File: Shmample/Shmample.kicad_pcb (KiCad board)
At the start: 2 copper layers, 127 x 127 mm, 149 parts, among them J1 Conn_01x04_Socket, J2 PowerOut, Q1 BC547, Q10 BC547, Q2 BC557, Q3 BC547, Q4 BC547, Q5 BC557, Q6 BC557, Q7 BC547, Q8 BC557, Q9 BC547, U1 358, U2 40106, U3 4015, U4 4066, U5 324, U6 LM7809_TO220, U7 4052, U8 358

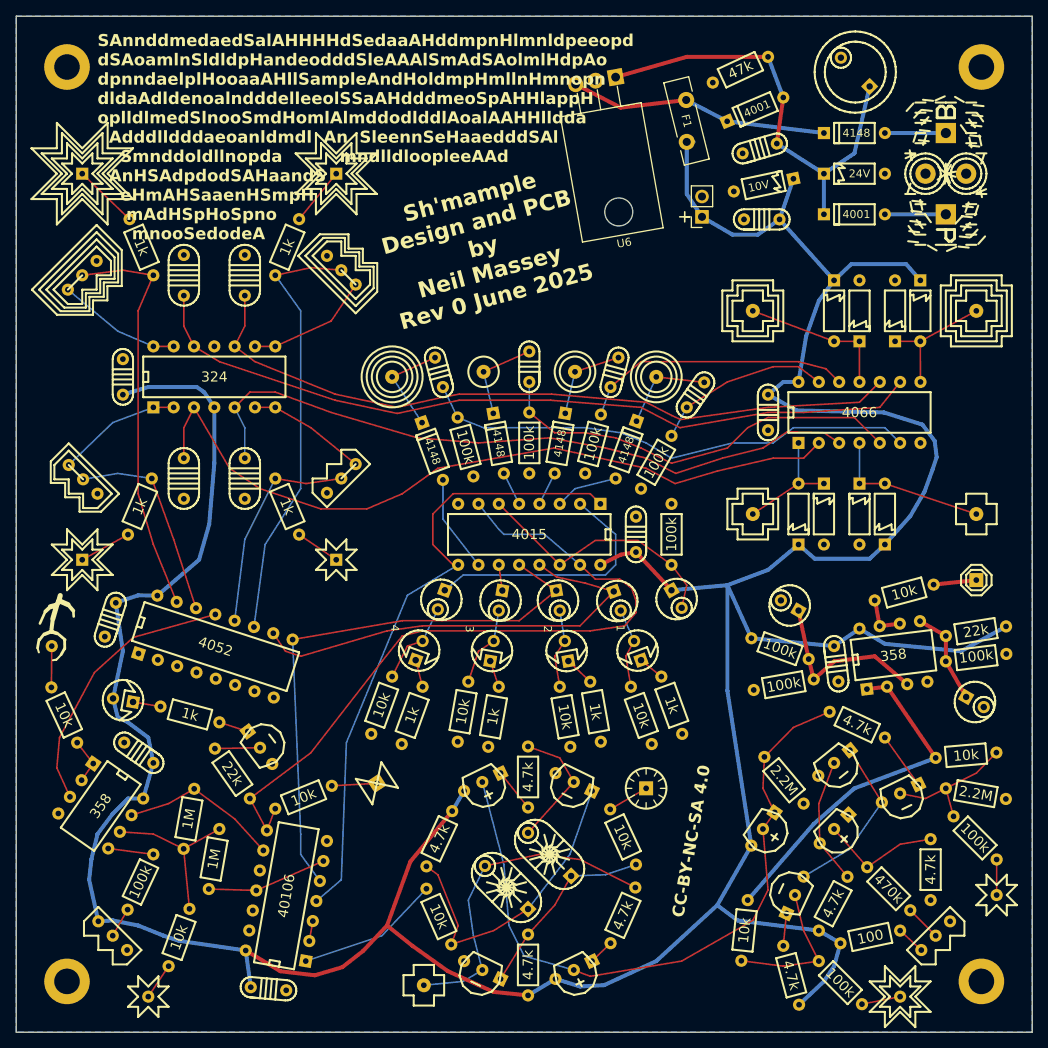
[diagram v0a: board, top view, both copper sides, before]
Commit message: ironed out some kinky tracks
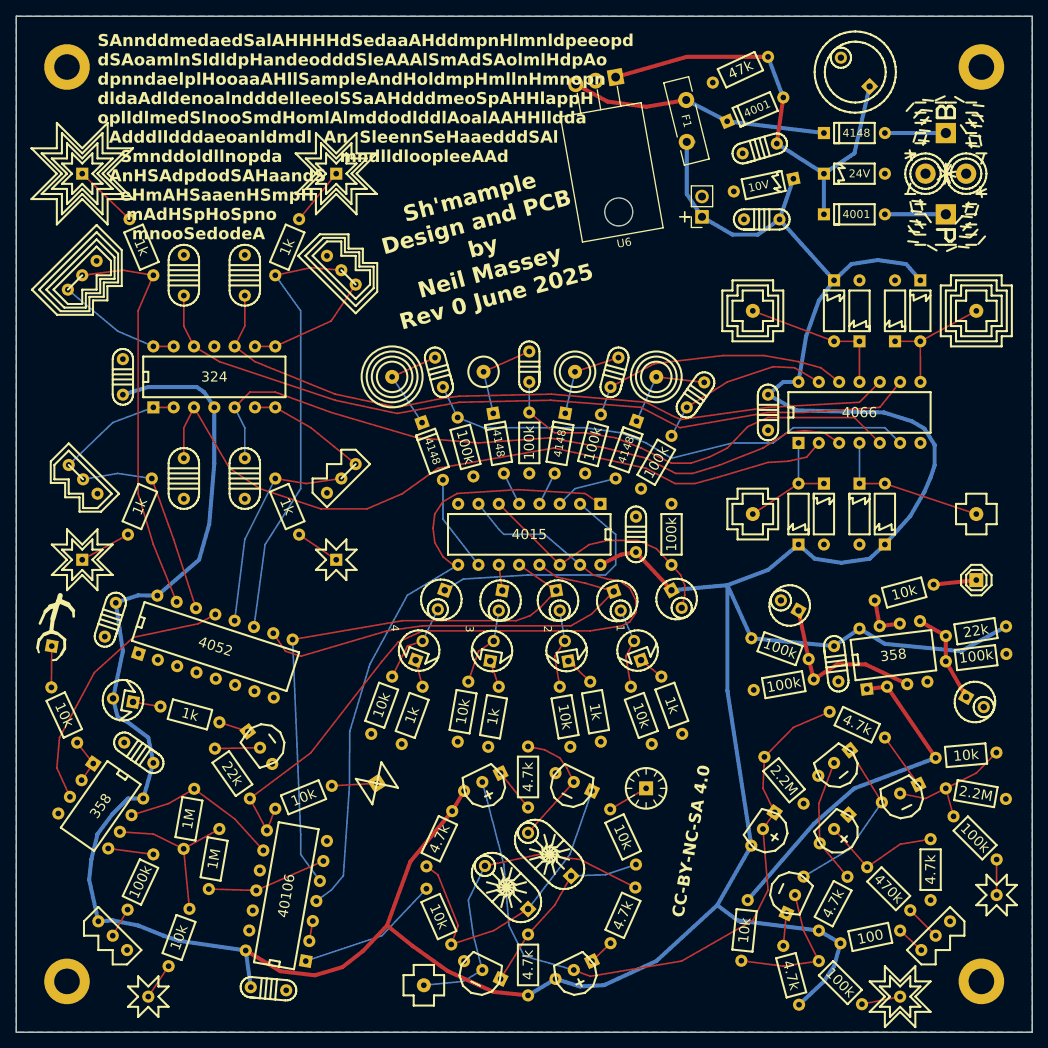
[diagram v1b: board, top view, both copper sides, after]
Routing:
- net Net-(U1A-+): track 22.7 -> 21.6 mm
- net Data: track 92.2 -> 91.6 mm

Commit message: Revision 1
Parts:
- removed C25, C26: 10uF, diy-nabra:cel1
- removed C27, C28: 100nF, diy-nabra:cpoly104_small
- removed J2: PowerOut, Connector_PinSocket_2.54mm:PinSocket_1x02_P2.54mm_Vertical
- removed TP20: Clk-Out, diy-nabra:wclk_out
- added C18: 10nF, diy-nabra:cpoly103, F.Cu at (93.3, 74.3)
- added D23: 9V1, diy-nabra:doz3, F.Cu at (102.9, 52.1)
- added PowerPos1: ThePowerOut, Connector_PinSocket_2.54mm:PinSocket_1x02_P2.54mm_Vertical, F.Cu at (105.4, 27.9)
- added Q11: BC547, diy-nabra:qnpn, F.Cu at (18.4, 87.0)
- added Q12: BC547, diy-nabra:qnpn, F.Cu at (18.4, 116.2)
- added Q13: BC547, diy-nabra:qnpn, F.Cu at (45.7, 117.5)
- added Q14: BC547, diy-nabra:qnpn, F.Cu at (18.4, 124.5)
- added R40: 100k, diy-nabra:r3, F.Cu at (43.2, 104.1)
- added R51: 100k, diy-nabra:r3, F.Cu at (73.0, 118.1)
- added R52: 47k, diy-nabra:r3, F.Cu at (82.5, 118.7)
- added R53: 22k, diy-nabra:r3, F.Cu at (79.4, 118.1)
- added R54: 10k, diy-nabra:r3, F.Cu at (76.2, 117.5)
- added R55: 1M, diy-nabra:r3, F.Cu at (63.8, 112.9)
- added R56: 22k, diy-nabra:r3, F.Cu at (23.5, 121.3)
- added R57: 1M, diy-nabra:r3, F.Cu at (67.7, 111.4)
- added R58: 1k, diy-nabra:r3, F.Cu at (31.1, 124.5)
- added R59: 22k, diy-nabra:r3, F.Cu at (88.6, 112.9)
- added R60: 10k, diy-nabra:r3, F.Cu at (88.9, 121.3)
- added R61: 1k, diy-nabra:r3, F.Cu at (61.0, 36.8)
- added R62: 1k, diy-nabra:r3, F.Cu at (73.7, 36.8)
- added R63: 1k, diy-nabra:r3, F.Cu at (86.4, 36.8)
- added R64: 1k, diy-nabra:r3, F.Cu at (99.1, 36.8)
- added R65: 10k, diy-nabra:r3, F.Cu at (57.7, 129.1)
- added R66: 100k, diy-nabra:r3, F.Cu at (96.4, 131.4)
- added R67: 100k, diy-nabra:r3, F.Cu at (87.6, 129.5)
- added R68: 100, diy-nabra:r3, F.Cu at (59.7, 50.2)
- added R69: 100, diy-nabra:r3, F.Cu at (73.0, 50.2)
- added R70: 100, diy-nabra:r3, F.Cu at (86.4, 50.2)
- added R71: 100, diy-nabra:r3, F.Cu at (100.3, 50.2)
- C1: value 10uF -> 2200uF; footprint diy-nabra:cel1 -> diy-nabra:cel2
- C10, C12: value 1uF -> *; footprint diy-nabra:cpoly105 -> diy-nabra:chairy
- C11, C9: value 1uF -> 10uF; footprint diy-nabra:cpoly105 -> diy-nabra:cel1
- C13: value 100nF -> 10uF; footprint diy-nabra:cpoly104_small -> diy-nabra:cel1
- C15, C16: value 100nF -> 10nF; footprint diy-nabra:cpoly104_small -> diy-nabra:cpoly103
- C17: value 10uF -> 10nF; footprint diy-nabra:cel1 -> diy-nabra:cpoly103
- C19: value 2200uF -> 1uF; footprint diy-nabra:cel2 -> diy-nabra:cpoly105
- C20, C21: value 100nF -> 1uF; footprint diy-nabra:cpoly104_small -> diy-nabra:cpoly105
- C22: value 10uF -> 1uF; footprint diy-nabra:cel1 -> diy-nabra:cpoly105
- C23: value 10uF -> 100nF; footprint diy-nabra:cel1 -> diy-nabra:cpoly104_small
- C3, C8: value * -> 100nF; footprint diy-nabra:chairy -> diy-nabra:cpoly104_small
- C4, C5, C6, C7: value 10nF -> 100nF; footprint diy-nabra:cpoly103 -> diy-nabra:cpoly104_small
- D1, D3: value LED -> 4001; footprint diy-nabra:led -> diy-nabra:do3
- D10, D12, D13: value 4148 -> LED; footprint diy-nabra:do3 -> diy-nabra:led
- D11: value 10V -> LED; footprint diy-nabra:doz3 -> diy-nabra:led
- D15: value 9V1 -> LED; footprint diy-nabra:doz3 -> diy-nabra:led
- D2: value LED -> 24V; footprint diy-nabra:led -> diy-nabra:doz3
- D4: value LED -> 4148; footprint diy-nabra:led -> diy-nabra:do3
- D5: value LED -> 10V; footprint diy-nabra:led -> diy-nabra:doz3
- D6, D7: value 4001 -> 4148
- D8: value 24V -> 4148; footprint diy-nabra:doz3 -> diy-nabra:do3
- R1: value 100k -> 47k
- R10, R29: value 4.7k -> 10k
- R11: value 1M -> 2.2M
- R12: value 4.7k -> 100k
- R13: value 10k -> 2.2M
- R14: value 2.2M -> 4.7k
- R16: value 2.2M -> 100k
- R19, R8: value 10k -> 4.7k
- R2: value 470k -> 100
- R20: value 4.7k -> 22k
- R22, R23: value 100k -> 10k
- R25, R26, R27, R28: value 1k -> 100k
- R30: value 22k -> 10k
- R31: value 47k -> 10k
- R32, R33, R34, R35, R36: value 1k -> 10k
- R37: value 22k -> 100k
- R39, R49, R50: value 10k -> 100k
- R4: value 100k -> 470k
- R41: value 100 -> 10k
- R45, R48: value 10k -> 1k
- R46: value 1M -> 1k
- R47: value 100k -> 1k
- R7: value 100k -> 4.7k
- RV3: value 4_W -> 1_W; footprint diy-nabra:wnob4 -> diy-nabra:wnob1
- RV4: value 3_W -> 2_W; footprint diy-nabra:wnob3 -> diy-nabra:wnob2
- RV5: value 2_W -> 3_W; footprint diy-nabra:wnob2 -> diy-nabra:wnob3
- RV6: value 1_W -> 4_W; footprint diy-nabra:wnob1 -> diy-nabra:wnob4
- TP10: value In-4 -> Rung; footprint diy-nabra:wsqu4in -> diy-nabra:wsqout
- TP11: value Out-4 -> In-1; footprint diy-nabra:wtrin4 -> diy-nabra:wsquin
- TP12: value Cmp-Out -> In-2; footprint diy-nabra:wcmp_out -> diy-nabra:wsqu2in
- TP13: value Hi -> In-3; footprint diy-nabra:wvout -> diy-nabra:wsqu3in
- TP14: value Pls-1 -> In-4; footprint diy-nabra:wcircin -> diy-nabra:wsqu4in
- TP15: value Pls-2 -> Out-1; footprint diy-nabra:wcirc2in -> diy-nabra:wtrin
- TP16: value Pls-3 -> Out-2; footprint diy-nabra:wcirc3in -> diy-nabra:wtrin2
- TP17: value Pls-4 -> Out-3; footprint diy-nabra:wcirc4in -> diy-nabra:wtrin3
- TP18: value Brown -> Out-4; footprint diy-nabra:wsquin -> diy-nabra:wtrin4
- TP19: footprint diy-nabra:wpod -> diy-nabra:wsqout
- TP2: value Data -> Ver
- TP3: value Ver -> Brown; footprint diy-nabra:wtrin -> diy-nabra:wsquin
- TP4: value In-1 -> Hi; footprint diy-nabra:wsquin -> diy-nabra:wvout
- TP5: value Out-1 -> Pls-1; footprint diy-nabra:wtrin -> diy-nabra:wcircin
- TP6: value In-3 -> Pls-2; footprint diy-nabra:wsqu2in -> diy-nabra:wcirc2in
- TP7: value Out-2 -> Pls-3; footprint diy-nabra:wtrin2 -> diy-nabra:wcirc3in
- TP8: value In-2 -> Pls-4; footprint diy-nabra:wsqu3in -> diy-nabra:wcirc4in
- TP9: value Out-3 -> Data; footprint diy-nabra:wtrin3 -> diy-nabra:wtrin
- U1: value 358 -> LM7809_TO220; footprint diy-nabra:dip8 -> Package_TO_SOT_THT:TO-220F-3_Horizontal_TabDown
- U2: value 40106 -> 358; footprint diy-nabra:dip14 -> diy-nabra:dip8
- U3: value 4015 -> 4066; footprint diy-nabra:dip16 -> diy-nabra:dip14
- U4: value 4066 -> LM324
- U5: value 324 -> 40106
- U6: value LM7809_TO220 -> LM324; footprint Package_TO_SOT_THT:TO-220-3_Horizontal_TabDown -> diy-nabra:dip14
- U7: value 4052 -> 4015
- U8: value 358 -> 4052; footprint diy-nabra:dip8 -> diy-nabra:dip16
- moved H1 161.6 mm to (133.3, 133.3)
- moved H2 161.6 mm to (19.1, 133.3)
- moved H3 114.3 mm to (133.3, 19.1)
- moved H4 114.3 mm to (19.1, 19.1)
- moved TP18 109.3 mm to (95.2, 29.2), turned to 0 degrees
- moved R38 108.8 mm to (20.3, 100.3), turned to 105 degrees
- moved C11 107.7 mm to (133.6, 97.9), turned to 115 degrees
- moved TP9 105.5 mm to (26.7, 134.6), turned to 90 degrees
- moved R1 103.7 mm to (109.3, 27.1), turned to -6 degrees
- moved D5 99.9 mm to (109.7, 42.0), turned to 20 degrees
- moved D15 97.8 mm to (36.1, 124.3), turned to 115 degrees
- moved TP2 96.5 mm to (125.7, 134.6)
- moved R37 93.9 mm to (43.2, 100.3), turned to 75 degrees
- moved R18 93.4 mm to (121.9, 53.3)
- moved R11 92.8 mm to (129.5, 120.7), turned to -65 degrees
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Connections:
- C1 pad 1: Net-(U1A-+) -> Net-(D1-K)
- C10 pad 1: Net-(U5A-+) -> Net-(Q7-C)
- C10 pad 2: GND -> Net-(Q9-B)
- C11 pad 1: Net-(U5C-+) -> Net-(U2B-+)
- C12 pad 1: Net-(U5D-+) -> Net-(Q9-C)
- C12 pad 2: GND -> Net-(Q7-B)
- C13 pad 1: GND -> +9V
- C13 pad 2: +9V -> RST
- C15 pad 1: GND -> Net-(C15-Pad1)
- C15 pad 2: +9V -> Net-(Q10-B)
- C16 pad 1: GND -> Net-(C16-Pad1)
- C16 pad 2: +9V -> Net-(Q11-B)
- C17 pad 1: Net-(U1B-+) -> Net-(C17-Pad1)
- C17 pad 2: GND -> Net-(Q12-B)
- C19 pad 1: Net-(D6-K) -> Net-(U6C-+)
- C2 pad 1: GND -> Net-(D1-K)
- C2 pad 2: +9V -> GND
- C20 pad 1: Net-(D6-K) -> Net-(U6D-+)
- C21 pad 1: +9V -> Net-(U6A-+)
- C22 pad 1: Q1 -> Net-(U6B-+)
- C22 pad 2: Net-(D1-A) -> GND
- C23 pad 1: Q2 -> +9V
- C23 pad 2: Net-(D2-A) -> GND
- C24 pad 1: Net-(U3B-Q3) -> Net-(U4B-+)
- C24 pad 2: Net-(D3-A) -> GND
- C3 pad 1: Net-(Q7-C) -> +9V
- C3 pad 2: Net-(Q9-B) -> GND
- C4 pad 1: Net-(D10-K) -> GND
- C4 pad 2: SW1 -> +9V
- C5 pad 1: Net-(D12-K) -> GND
- C5 pad 2: SW2 -> +9V
- C6 pad 1: Net-(D13-K) -> GND
- C6 pad 2: SW3 -> +9V
- C7 pad 1: Net-(D14-K) -> GND
- C7 pad 2: SW4 -> +9V
- C8 pad 1: Net-(Q9-C) -> GND
- C8 pad 2: Net-(Q7-B) -> +9V
- C9 pad 1: Net-(U5B-+) -> Net-(U2A-+)
- D10 pad 1: Net-(D10-K) -> GND
- D11 pad 1: +9V -> GND
- D11 pad 2: GND -> Net-(D11-A)
- D12 pad 1: Net-(D12-K) -> GND
- D13 pad 1: Net-(D13-K) -> GND
- D15 pad 2: GND -> +9V
- D16 pad 2: Net-(D15-K) -> Net-(D16-A)
- D17 pad 1: +9V -> Net-(D16-A)
- D17 pad 2: Net-(D17-A) -> GND
- D18 pad 1: Net-(D17-A) -> +9V
- D18 pad 2: GND -> Net-(D18-A)
- D19 pad 1: +9V -> Net-(D18-A)
- D19 pad 2: Net-(D19-A) -> GND
- D2 pad 1: Net-(D2-K) -> Net-(D1-K)
- D2 pad 2: Net-(D2-A) -> GND
- D20 pad 1: Net-(D19-A) -> +9V
- D20 pad 2: GND -> Net-(D20-A)
- D21 pad 1: +9V -> Net-(D20-A)
- D21 pad 2: Net-(D21-A) -> GND
- D22 pad 1: Net-(D21-A) -> +9V
- D22 pad 2: GND -> Net-(D22-A)
- D3 pad 2: Net-(D3-A) -> Net-(D1-K)
- D4 pad 1: Net-(D4-K) -> Net-(D3-K)
- D4 pad 2: Net-(D4-A) -> Batt
- D5 pad 1: Net-(D5-K) -> +9V
- D5 pad 2: +9V -> GND
- D6 pad 2: Net-(D6-A) -> Q1A
- D7 pad 2: Net-(D6-K) -> Q2A
- D8 pad 1: Net-(D6-K) -> Net-(D8-K)
- D8 pad 2: GND -> Q3A
- D9 pad 1: Net-(D7-K) -> Net-(D9-K)
- D9 pad 2: Batt -> Q4B
- F1 pad 1: Net-(D7-K) -> Net-(D3-K)
- J1 pad 1: Net-(D6-A) -> Net-(D1-A)
- R1 pad 1: Net-(R1-Pad1) -> Net-(D1-K)
- R1 pad 2: Net-(Q1-B) -> GND
- R10 pad 1: Net-(Q2-E) -> Net-(Q4-B)
- R10 pad 2: +9V -> MIDO
- R11 pad 1: Net-(U8B--) -> GND
- R11 pad 2: Net-(R11-Pad2) -> Net-(Q4-B)
- R12 pad 1: Net-(Q4-C) -> Net-(Q4-B)
- R12 pad 2: Net-(Q5-B) -> Net-(R12-Pad2)
- R13 pad 1: Net-(Q4-B) -> GND
- R13 pad 2: MIDO -> Net-(Q5-B)
- R14 pad 1: GND -> Net-(Q7-B)
- R14 pad 2: Net-(Q4-B) -> Net-(Q6-C)
- R15 pad 1: Net-(Q4-B) -> Net-(U2A-+)
- R15 pad 2: Net-(R15-Pad2) -> +9V
- R16 pad 2: Net-(Q5-B) -> Net-(U2A-+)
- R17 pad 1: Net-(Q7-B) -> Net-(Q7-C)
- R17 pad 2: Net-(Q6-C) -> +9V
- R18 pad 1: Net-(Q7-C) -> Net-(Q9-B)
- R18 pad 2: +9V -> Net-(Q8-C)
- R19 pad 2: Pulse -> +9V
- R2 pad 2: Net-(Q2-B) -> +9V
- R20 pad 1: Net-(Q9-B) -> Net-(U2B-+)
- R20 pad 2: Net-(Q8-C) -> +9V
- R21 pad 2: SW1 -> Net-(U2B-+)
- R22 pad 1: GND -> Net-(Q9-C)
- R22 pad 2: SW2 -> Pulse
- R23 pad 1: GND -> Net-(R23-Pad1)
- R23 pad 2: SW3 -> Hi
- R24 pad 2: SW4 -> RST
- R25 pad 1: Net-(D1-K) -> GND
- R25 pad 2: GND -> Net-(D6-K)
- R26 pad 1: Net-(D2-K) -> Net-(D7-K)
- R27 pad 1: Net-(D3-K) -> Net-(D8-K)
- R28 pad 1: Net-(D4-K) -> Net-(D9-K)
- R29 pad 1: Net-(Q9-C) -> Net-(D6-K)
- R29 pad 2: +9V -> Net-(C15-Pad1)
- R3 pad 1: Net-(U1A-+) -> Net-(R3-Pad1)
- R3 pad 2: +9V -> Net-(Q1-B)
- R30 pad 1: Net-(Q10-B) -> Net-(D7-K)
- R30 pad 2: Data -> Net-(C16-Pad1)
- R31 pad 1: Net-(D6-K) -> Net-(D8-K)
- R31 pad 2: GND -> Net-(C17-Pad1)
- R32 pad 1: Net-(Q10-C) -> Net-(D9-K)
- R32 pad 2: Net-(D5-K) -> Net-(C18-Pad1)
- R33 pad 1: Net-(U7-X0) -> Net-(C15-Pad1)
- R34 pad 1: Net-(U7-X1) -> Net-(R34-Pad1)
- R34 pad 2: Net-(R34-Pad2) -> Net-(C16-Pad1)
- R35 pad 1: Net-(U7-X3) -> Net-(R35-Pad1)
- R35 pad 2: Net-(R35-Pad2) -> Net-(C17-Pad1)
- R36 pad 1: Net-(U7-X2) -> Net-(R36-Pad1)
- R36 pad 2: Net-(R36-Pad2) -> Net-(C18-Pad1)
- R37 pad 1: Net-(U1B-+) -> Net-(Q10-B)
- R37 pad 2: +9V -> GND
- R38 pad 1: GND -> Net-(Q11-B)
- R38 pad 2: Net-(U1B-+) -> GND
- R39 pad 1: Net-(Q7-C) -> Net-(Q12-B)
- R39 pad 2: Net-(R39-Pad2) -> GND
- R4 pad 1: GND -> Net-(R4-Pad1)
- R4 pad 2: Net-(U1A-+) -> Net-(Q2-B)
- R41 pad 1: Net-(R41-Pad1) -> Net-(Q10-C)
- R42 pad 1: Net-(D1-A) -> Net-(Q11-C)
- R42 pad 2: GND -> +9V
- R43 pad 1: Net-(D2-A) -> Net-(Q12-C)
- R43 pad 2: GND -> +9V
- R44 pad 1: Net-(D3-A) -> Net-(Q13-C)
- R44 pad 2: GND -> +9V
- R45 pad 1: Net-(D4-A) -> Net-(D10-A)
- R45 pad 2: GND -> Q1B
- R46 pad 1: Net-(U8B--) -> Net-(D11-A)
- R46 pad 2: Net-(R46-Pad2) -> Q2B
- R47 pad 1: GND -> Net-(D12-A)
- R47 pad 2: RST -> Q3B
- R48 pad 1: Net-(U8A--) -> Net-(D13-A)
- R48 pad 2: Net-(R48-Pad2) -> Q4A
- R49 pad 2: Data -> Net-(U4D-+)
- R50 pad 2: Hi -> Net-(U4D--)
- R7 pad 1: Net-(R7-Pad1) -> Net-(Q1-C)
- R7 pad 2: Net-(U8B-+) -> +9V
- R8 pad 1: Net-(R8-Pad1) -> Net-(Q2-E)
- R8 pad 2: Net-(U8B--) -> +9V
- R9 pad 1: Net-(Q1-C) -> Net-(Q4-C)
- R9 pad 2: +9V -> Net-(Q5-B)
- RV1 pad 2: Net-(R2-Pad1) -> Net-(R4-Pad1)
- RV1 pad 3: Net-(R41-Pad1) -> Net-(R2-Pad1)
- RV2 pad 2: Net-(R7-Pad1) -> Net-(R49-Pad1)
- RV3 pad 2: Net-(U7-X2) -> Net-(U8-X0)
- RV3 pad 3: Net-(U5D--) -> Net-(U6C--)
- RV4 pad 2: Net-(U7-X3) -> Net-(U8-X1)
- RV4 pad 3: Net-(U5C--) -> Net-(U6D--)
- RV5 pad 2: Net-(U7-X1) -> Net-(U8-X3)
- RV5 pad 3: Net-(U5A--) -> Net-(U6A--)
- RV6 pad 2: Net-(U7-X0) -> Net-(U8-X2)
- RV6 pad 3: Net-(U5B--) -> Net-(U6B--)
- TP1 pad 1: Net-(R1-Pad1) -> Net-(R3-Pad1)
- TP10 pad 1: Net-(D21-A) -> Net-(R60-Pad1)
- TP11 pad 1: Net-(R36-Pad2) -> IN1
- TP12 pad 1: Net-(R49-Pad1) -> IN2
- TP13 pad 1: Net-(R50-Pad1) -> IN3
- TP14 pad 1: Net-(D10-K) -> IN4
- TP15 pad 1: Net-(D12-K) -> Net-(R61-Pad2)
- TP16 pad 1: Net-(D13-K) -> Net-(R62-Pad2)
- TP17 pad 1: Net-(D14-K) -> Net-(R63-Pad2)
- TP18 pad 1: Net-(Q7-B) -> Net-(R64-Pad2)
- TP19 pad 1: Net-(R48-Pad2) -> Net-(R65-Pad2)
- TP2 pad 1: Net-(R8-Pad1) -> Net-(R12-Pad2)
- TP3 pad 1: Net-(R15-Pad2) -> Net-(Q7-B)
- TP4 pad 1: Net-(D15-K) -> Net-(R23-Pad1)
- TP6 pad 1: Net-(D17-A) -> Net-(R34-Pad1)
- TP7 pad 1: Net-(R34-Pad2) -> Net-(R35-Pad1)
- TP8 pad 1: Net-(D19-A) -> Net-(R36-Pad1)
- TP9 pad 1: Net-(R35-Pad2) -> Net-(R50-Pad1)
- U1 pad 1: MIDO -> Net-(D1-K)
- U1 pad 2: MIDO -> GND
- U1 pad 3: Net-(U1A-+) -> Net-(D3-K)
- U2 pad 1: Pulse -> MIDO
- U2 pad 2: Net-(U2-Pad2) -> MIDO
- U2 pad 3: Net-(U2-Pad2) -> Net-(U2A-+)
- U2 pad 4: Net-(U3A-CP) -> GND
- U2 pad 5: Q2 -> Net-(U2B-+)
- U2 pad 6: Net-(R11-Pad2) -> Hi
- U2 pad 7: GND -> Hi
- U2 pad 8: Data -> +9V
- U3 pad 1: Net-(U3A-CP) -> Net-(D22-A)
- U3 pad 10: Net-(D14-A) -> Net-(U6C-+)
- U3 pad 11: Net-(U3B-Q3) -> Net-(D16-A)
- U3 pad 12: Q2 -> SW1
- U3 pad 13: Q1 -> SW4
- U3 pad 14: RST -> +9V
- U3 pad 2: Net-(U3B-Q4) -> Net-(U6B-+)
- U3 pad 3: Net-(D13-A) -> Net-(U6A-+)
- U3 pad 4: Net-(D12-A) -> Net-(D20-A)
- U3 pad 5: Net-(D10-A) -> SW3
- U3 pad 6: RST -> SW2
- U3 pad 7: Data -> GND
- U3 pad 8: GND -> Net-(D18-A)
- U3 pad 9: Net-(U3A-CP) -> Net-(U6D-+)
- U4 pad 1: Net-(D17-A) -> Net-(U4A--)
- U4 pad 10: Net-(U5C-+) -> MIDO2
- U4 pad 11: Net-(D19-A) -> GND
- U4 pad 12: SW2 -> Net-(U4D-+)
- U4 pad 13: SW3 -> Net-(U4D--)
- U4 pad 14: +9V -> Net-(R57-Pad2)
- U4 pad 2: Net-(U5A-+) -> Net-(U4A--)
- U4 pad 3: Net-(U5B-+) -> Net-(U4A-+)
- U4 pad 4: Net-(D15-K) -> +9V
- U4 pad 5: SW1 -> Net-(U4B-+)
- U4 pad 6: SW4 -> MIDO2
- U4 pad 7: GND -> MIDO2
- U4 pad 8: Net-(D21-A) -> Net-(R59-Pad2)
- U4 pad 9: Net-(U5D-+) -> Net-(U4C--)
- U5 pad 1: Net-(U5A--) -> Net-(Q11-C)
- U5 pad 10: Net-(U5C-+) -> SW4
- U5 pad 11: GND -> Net-(Q13-C)
- U5 pad 12: Net-(U5D-+) -> SW1
- U5 pad 13: Net-(U5D--) -> Net-(Q10-C)
- U5 pad 14: Net-(U5D--) -> +9V
- U5 pad 2: Net-(U5A--) -> SW2
- U5 pad 3: Net-(U5A-+) -> Net-(Q12-C)
- U5 pad 4: +9V -> SW3
- U5 pad 5: Net-(U5B-+) -> Net-(R57-Pad2)
- U5 pad 6: Net-(U5B--) -> Data
- U5 pad 7: Net-(U5B--) -> GND
- U5 pad 8: Net-(U5C--) -> Net-(D14-A)
- U5 pad 9: Net-(U5C--) -> Q2A
- U6 pad 1: Net-(D6-K) -> Net-(U6A--)
- U6 pad 2: GND -> Net-(U6A--)
- U6 pad 3: Net-(D7-K) -> Net-(U6A-+)
- U7 pad 1: GND -> Pulse
- U7 pad 10: Q1 -> Q4A
- U7 pad 11: Net-(U7-X3) -> Q3B
- U7 pad 12: Net-(U7-X0) -> Q2B
- U7 pad 13: Net-(U7-X) -> Q1B
- U7 pad 14: Net-(U7-X1) -> RST
- U7 pad 15: Net-(U7-X2) -> Data
- U7 pad 2: GND -> Q4B
- U7 pad 3: unconnected-(U7-Y-Pad3) -> Q3A
- U7 pad 4: GND -> Q2A
- U7 pad 5: GND -> Q1A
- U7 pad 6: GND -> RST
- U7 pad 7: GND -> Data
- U7 pad 9: Q2 -> Pulse
- U8 pad 1: Net-(U8A--) -> GND
- U8 pad 2: Net-(U8A--) -> GND
- U8 pad 3: Net-(U7-X) -> unconnected-(U8-Y-Pad3)
- U8 pad 5: Net-(U8B-+) -> GND
- U8 pad 6: Net-(U8B--) -> GND
- U8 pad 7: Net-(R46-Pad2) -> GND
- U8 pad 8: +9V -> GND
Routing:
- net Q2A: track 0.00 -> 133.3 mm
- net Net-(U4A-+): track 0.00 -> 119.9 mm
- net Net-(D22-A): track 0.00 -> 112.7 mm
- net Net-(U5D-+): track 98.9 -> 0.00 mm
- net Net-(Q12-B): track 0.00 -> 98.5 mm
- net +9V: track 456.7 -> 552.0 mm
- net Q1A: track 0.00 -> 95.1 mm
- net Net-(U5A-+): track 93.9 -> 0.00 mm
- net Net-(U5C-+): track 90.8 -> 0.00 mm
- net Net-(D20-A): track 0.00 -> 90.2 mm
- net Net-(U5B-+): track 86.2 -> 0.00 mm
- net Net-(U6A--): track 0.00 -> 85.0 mm
- net Net-(U6B--): track 0.00 -> 84.7 mm
- net Net-(U3A-CP): track 78.8 -> 0.00 mm
- net Q2: track 71.2 -> 0.00 mm
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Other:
- board text added: "Sh'mample Design and PCB by Neil Massey Rev 1 Nov 2025"
- board text removed: "1"
- board text removed: "2"
- board text removed: "3"
- board text removed: "4"
- board text removed: "SAnnddmedaedSalAHHHHdSedaaAHddmpnHlmnldpeeopd dSAoamlnSldldpHandeodddSleAAAlSmAdSAolmlHdpAo dpnndaelplHooaaAHllSampleAndHoldmpHmllnHmnopn dldaAdldenoalndddelleeolSSaAHdddmeoSpAHHlappH oplldlmedSlnooSmdHomlAlmddodlddlAoalAAHHlldda Adddlldddaeoanldmdl An SleennSeHaaedddSAl Smnddoldllnopda mndlldloopleeAAd AnHSAdpdodSAHaandS eHmAHSaaenHSmpH mAdHSpHoSpno mnooSedodeA"
- board text removed: "Sh'mample Design and PCB by Neil Massey Rev 0 June 2025"

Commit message: Big Pads
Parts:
- removed C11: 10uF, diy-nabra:cel1
- removed R2: 100, diy-nabra:r3
- R20: value 22k -> 100k
- R21: value 100k -> 10k
- R66: value 100k -> 22k
- U4, U6: value LM324 -> 324
- moved TP4 66.2 mm to (99.1, 134.6)
- moved R23 64.9 mm to (87.0, 136.5), turned to 170 degrees
- moved R4 3.17 mm to (113.7, 123.8), turned to -66 degrees
- moved R6 1.33 mm to (122.4, 123.8), turned to -113 degrees
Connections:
- R22 pad 2: Pulse -> RollO
- R23 pad 1: Net-(R23-Pad1) -> Hi
- R23 pad 2: Hi -> Net-(R23-Pad2)
- RV1 pad 3: Net-(R2-Pad1) -> +9V
- TP4 pad 1: Net-(R23-Pad1) -> Net-(R23-Pad2)
- U2 pad 6: Hi -> RollO
- U2 pad 7: Hi -> Pulse
- U4 pad 10: MIDO2 -> MIDO
- U4 pad 6: MIDO2 -> Hi
- U4 pad 7: MIDO2 -> Hi
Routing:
- net MIDO: track 49.3 -> 90.5 mm
- net RollO: track 0.00 -> 28.2 mm
- net +9V: track 552.0 -> 573.1 mm
- net Net-(R2-Pad1): track 13.1 -> 0.00 mm
- net Net-(R23-Pad2): track 0.00 -> 12.7 mm
- net MIDO2: track 10.6 -> 0.00 mm
- net Net-(U2B-+): track 12.6 -> 6.96 mm
- net Net-(R23-Pad1): track 4.10 -> 0.00 mm
- net Net-(Q2-B): track 13.9 -> 16.6 mm
- net Hi: track 5.93 -> 7.28 mm
- net Pulse: track 63.4 -> 64.5 mm

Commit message: Added shmatic
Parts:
- added J2: Barrel_Jack_Switch, Connector_BarrelJack:BarrelJack_Horizontal, F.Cu at (123.2, 27.0)
- TP10: footprint diy-nabra:wsqout -> diy-nabra:wsqu2in
- TP19: value All-Out -> Select-Out
- moved C1 12.2 mm to (111.1, 15.9)
- moved D1 3.81 mm to (119.5, 42.0)
- moved D4 3.34 mm to (119.4, 31.8), turned to 0 degrees
- moved D2 3.18 mm to (119.4, 36.6)
- moved C2 2.03 mm to (109.2, 36.8)
- moved R1 1.31 mm to (108.0, 27.1)
- moved D3 1.27 mm to (108.0, 31.8)
- moved TP10 0.90 mm to (97.2, 117.5), turned to 57 degrees
- moved PowerPos1 0.63 mm to (104.8, 27.9)
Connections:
- J1 pad 1: Net-(D1-A) -> Net-(J1-Pin_1)
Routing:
- net Net-(J1-Pin_1): track 0.00 -> 29.8 mm
- net Net-(D1-A): track 6.84 -> 14.4 mm
- net Net-(D3-K): track 49.9 -> 54.3 mm
- net Net-(D1-K): track 66.8 -> 65.5 mm
- net Net-(R60-Pad1): track 4.64 -> 5.51 mm
- net Batt: track 6.35 -> 6.94 mm
- net Net-(U4D--): track 32.1 -> 32.6 mm
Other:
- board text added: "Sh'mample Design and PCB by Neil Massey Rev 1 Jan 2026"
- board text removed: "Sh'mample Design and PCB by Neil Massey Rev 1 Nov 2025"

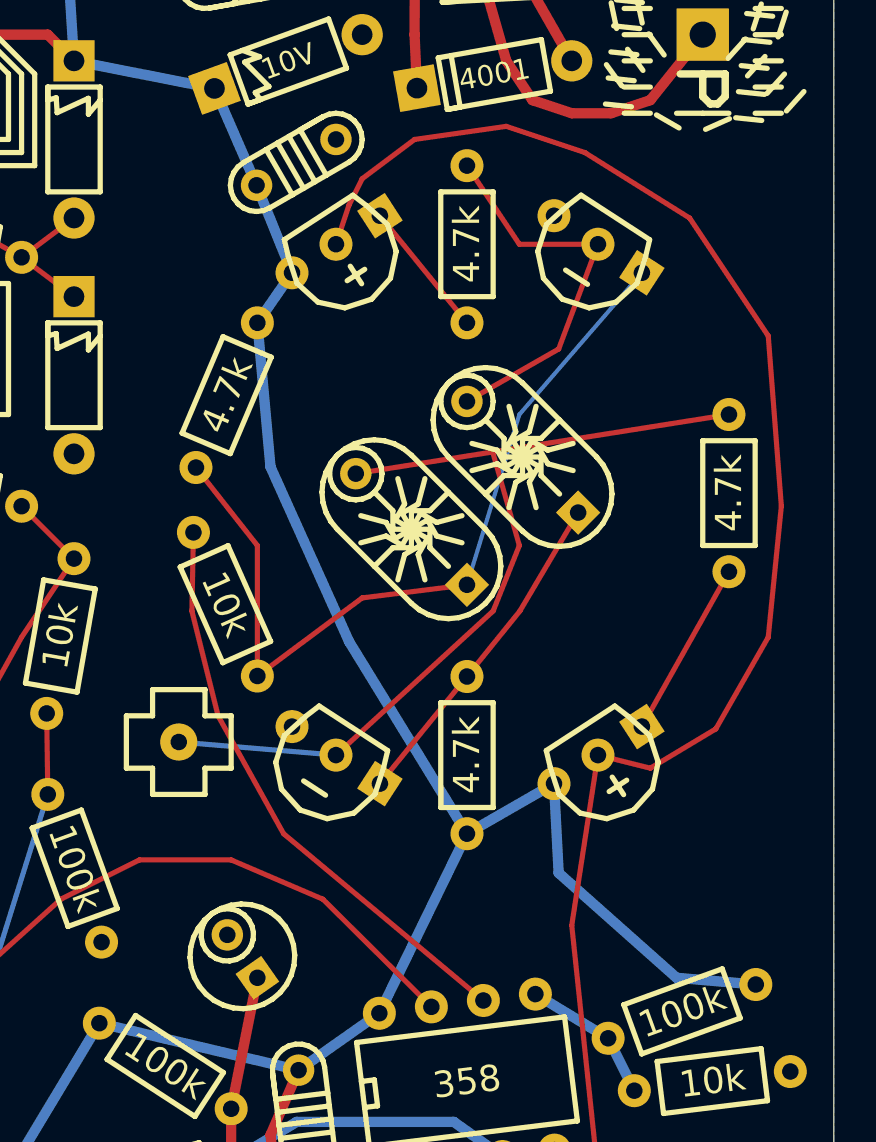
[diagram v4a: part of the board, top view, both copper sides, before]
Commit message: Just moved the rollz down a bit
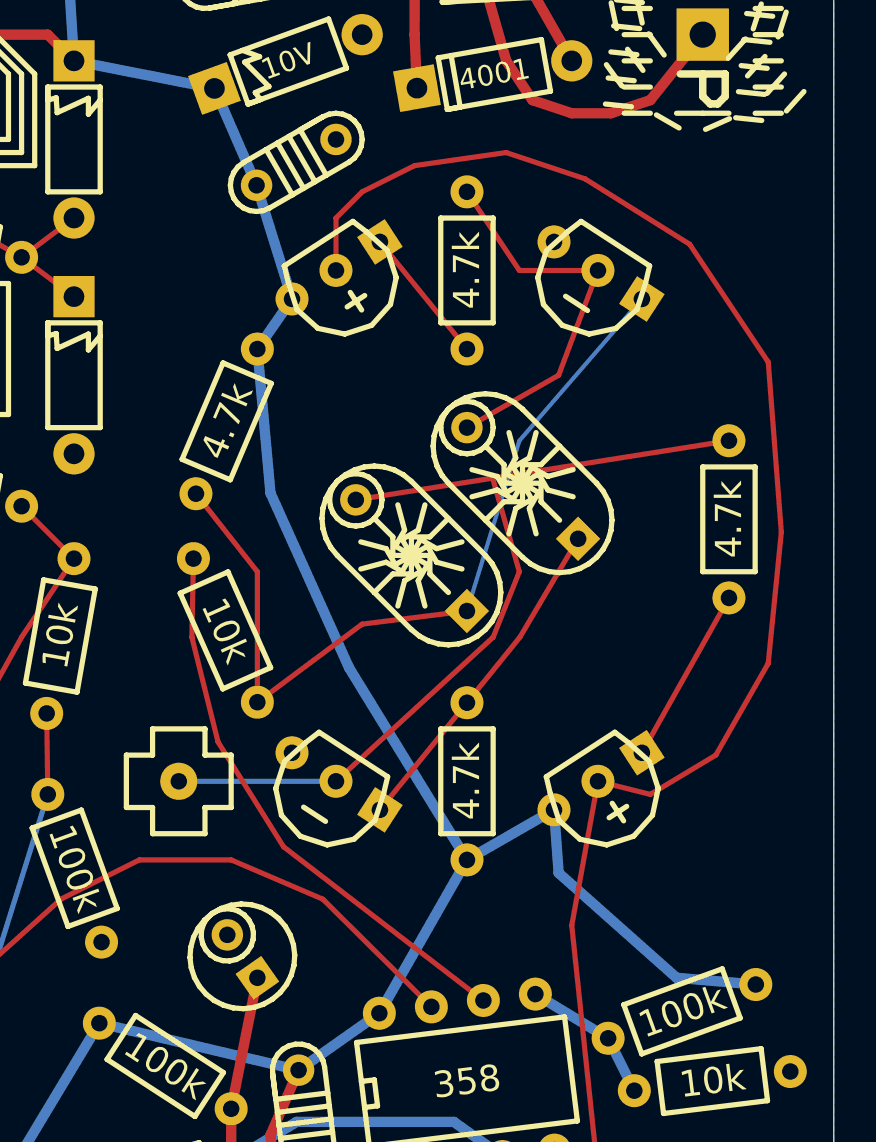
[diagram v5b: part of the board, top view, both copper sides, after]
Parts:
- moved TP3 1.91 mm to (108.0, 75.6)
- moved C10 1.27 mm to (121.9, 58.4)
- moved C12 1.27 mm to (116.5, 61.9)
- moved Q6 1.27 mm to (128.3, 75.6)
- moved Q7 1.27 mm to (115.6, 75.6)
- moved Q8 1.27 mm to (115.6, 50.8)
- moved Q9 1.27 mm to (128.3, 50.8)
- moved R14 1.27 mm to (134.6, 66.7)
- moved R17 1.27 mm to (121.9, 79.4)
- moved R18 1.27 mm to (121.9, 54.6)
- moved R19 1.27 mm to (111.8, 54.6)
- moved R22 1.27 mm to (108.7, 64.8)
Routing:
- net +9V: track 573.1 -> 571.9 mm
- net RollO: track 28.2 -> 27.3 mm
- net Net-(Q5-B): track 104.2 -> 103.6 mm

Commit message: Final revision of revision 1 before manufacture
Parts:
- removed the R22 at (108.7, 64.8)
- added C11: 22uF, diy-nabra:cel1, F.Cu at (66.2, 92.3)
- added C25: 22uF, diy-nabra:cel1, F.Cu at (73.2, 92.1)
- added C26: 22uF, diy-nabra:cel1, F.Cu at (80.2, 92.1)
- added C27: 22uF, diy-nabra:cel1, F.Cu at (87.0, 92.1)
- added C28: 100uF, diy-nabra:cel2, F.Cu at (43.2, 22.9)
- added D24: LED, diy-nabra:led, F.Cu at (17.8, 26.0)
- added D25: LED, diy-nabra:led, F.Cu at (17.8, 33.7)
- added D26: LED, diy-nabra:led, F.Cu at (17.8, 41.3)
- added D27: LED, diy-nabra:led, F.Cu at (17.8, 48.9)
- added R2: 1k, diy-nabra:r3, F.Cu at (15.2, 55.2)
- added R47: 1k, diy-nabra:r3, F.Cu at (80.0, 85.1)
- added R72: 10k, diy-nabra:r3, F.Cu at (75.6, 88.3)
- added R73: 10k, diy-nabra:r3, F.Cu at (87.6, 88.3)
- added R74: 10k, diy-nabra:r3, F.Cu at (99.7, 88.3)
- R22: renamed from R47; value 1k -> 10k
- R51: value 100k -> 1M
- R59: value 22k -> 4.7k
- R8: value 4.7k -> 470k
- TP12: footprint diy-nabra:wsqu2in -> diy-nabra:wsqout
- moved PowerPos1 53.1 mm to (52.7, 17.8)
- moved R22 16.9 mm to (63.5, 88.3), turned to 180 degrees
- moved R45 16.6 mm to (55.9, 85.1), turned to 0 degrees
- moved R46 11.3 mm to (67.9, 85.1), turned to 0 degrees
- moved R48 11.3 mm to (92.1, 85.1), turned to 0 degrees
- moved R19 5.12 mm to (109.2, 59.1), turned to -90 degrees
- moved C21 5.08 mm to (19.7, 55.2), turned to 30 degrees
- moved R25 1.27 mm to (62.2, 74.9)
- moved R26 1.27 mm to (77.5, 82.1)
- moved R27 1.27 mm to (90.2, 82.1)
- moved R28 1.27 mm to (104.2, 82.1)
- moved D15 0.88 mm to (36.7, 123.7), turned to 135 degrees
- moved R21 0.28 mm to (130.2, 90.8), turned to -33 degrees
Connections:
- C12 pad 1: Net-(Q9-C) -> RollO
- D10 pad 1: GND -> Net-(D10-K)
- D11 pad 1: GND -> Net-(D11-K)
- D12 pad 1: GND -> Net-(D12-K)
- D13 pad 1: GND -> Net-(D13-K)
- J1 pad 1: Net-(J1-Pin_1) -> Net-(D1-A)
- J2 pad 3: Net-(J1-Pin_1) -> unconnected-(J2-Pad3)
- Q9 pad 1: Net-(Q9-C) -> RollO
- R19 pad 1: Net-(Q9-C) -> RollO
- R22 pad 1: Net-(D12-A) -> Net-(D10-A)
- R22 pad 2: Q3B -> GND
- R45 pad 1: Net-(D10-A) -> GND
- R45 pad 2: Q1B -> Net-(D10-K)
- R46 pad 1: Net-(D11-A) -> GND
- R46 pad 2: Q2B -> Net-(D11-K)
- R48 pad 1: Net-(D13-A) -> GND
- R48 pad 2: Q4A -> Net-(D13-K)
- U8 pad 1: GND -> Y0
- U8 pad 2: GND -> Y2
- U8 pad 3: unconnected-(U8-Y-Pad3) -> +9V
- U8 pad 4: GND -> Y3
- U8 pad 5: GND -> Y1
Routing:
- net Net-(Q9-C): track 40.3 -> 0.00 mm
- net Y2: track 0.00 -> 32.4 mm
- net Net-(J1-Pin_1): track 29.8 -> 0.00 mm
- net Net-(D24-K): track 0.00 -> 29.7 mm
- net RollO: track 27.3 -> 56.0 mm
- net Y3: track 0.00 -> 13.9 mm
- net +9V: track 571.9 -> 584.8 mm
- net Net-(Q13-B): track 68.7 -> 81.4 mm
- net Net-(D11-A): track 6.07 -> 14.5 mm
- net Y0: track 0.00 -> 8.28 mm
- net Net-(D10-A): track 10.7 -> 18.8 mm
- net Y1: track 0.00 -> 7.65 mm
- net Net-(D12-K): track 0.00 -> 7.62 mm
- net Net-(D13-K): track 0.00 -> 7.32 mm
- net Net-(D10-K): track 0.00 -> 7.18 mm
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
